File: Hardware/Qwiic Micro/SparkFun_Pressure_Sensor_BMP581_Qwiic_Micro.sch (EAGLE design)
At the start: 28 parts, among them J1 QWIIC_RIGHT_ANGLE, U1 BMP581

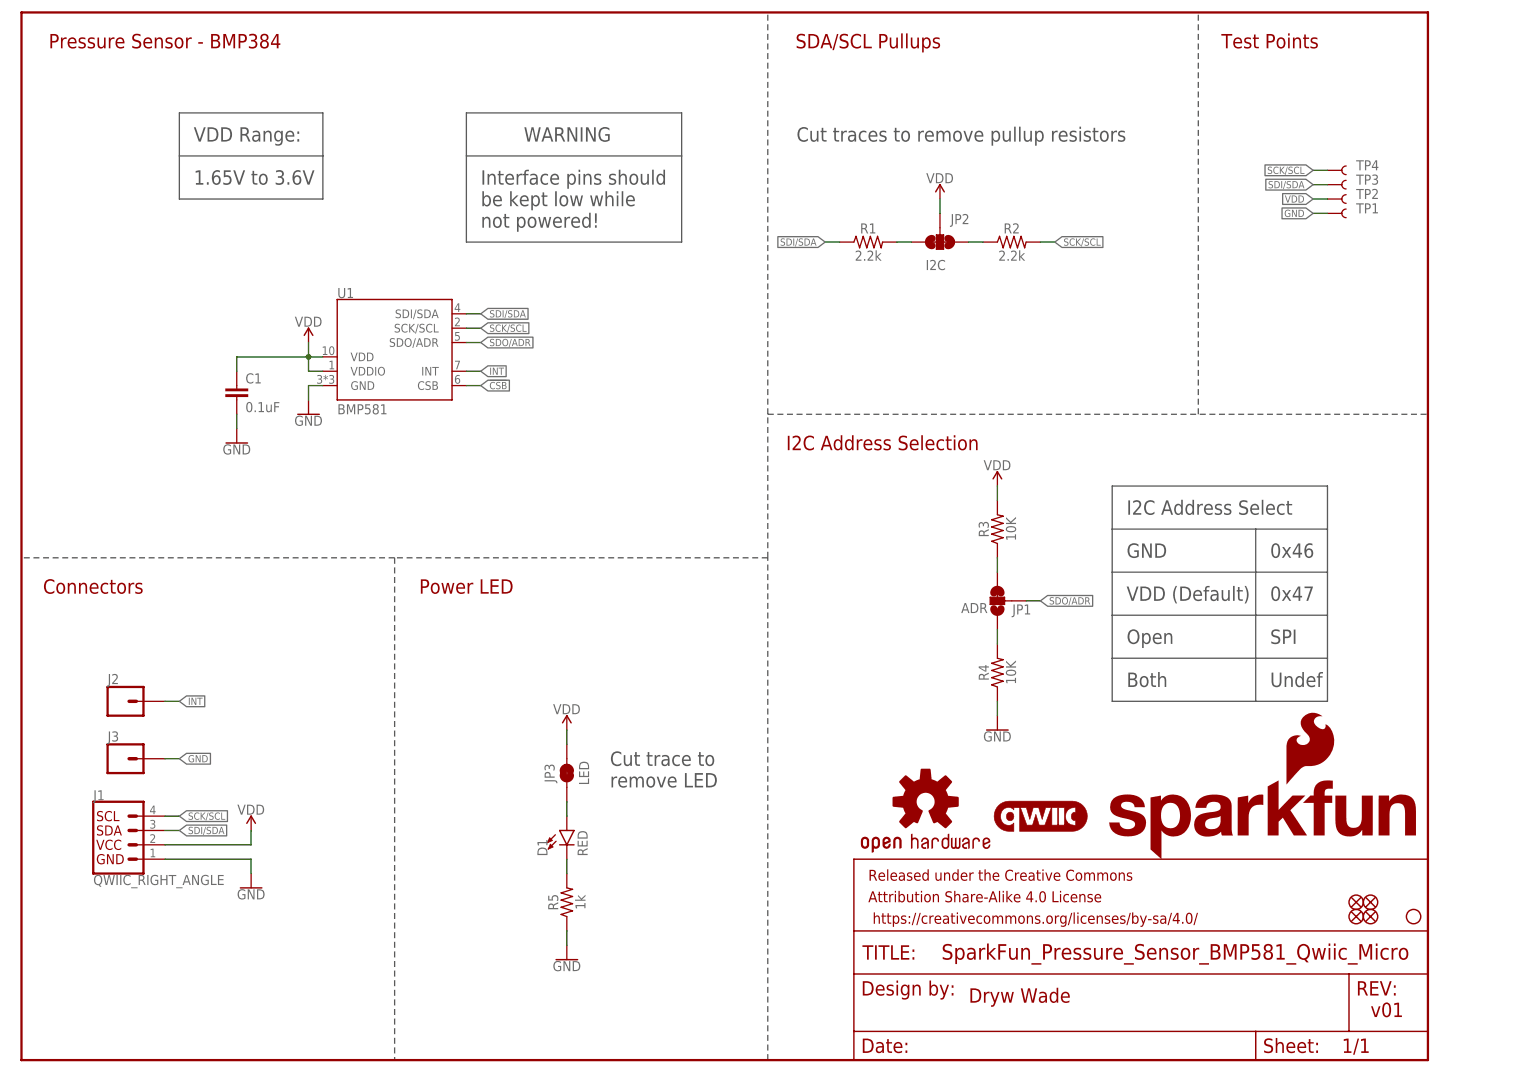
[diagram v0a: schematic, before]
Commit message: Design review updates
Rename files
Change to v10 (accelerating to reds)
Fix sensor name in schematic
Add note to schematic about max wire diameter in Micro PTH connectors
Update VDD range
Fix acid trap in Micro
Move PWR LED to give space
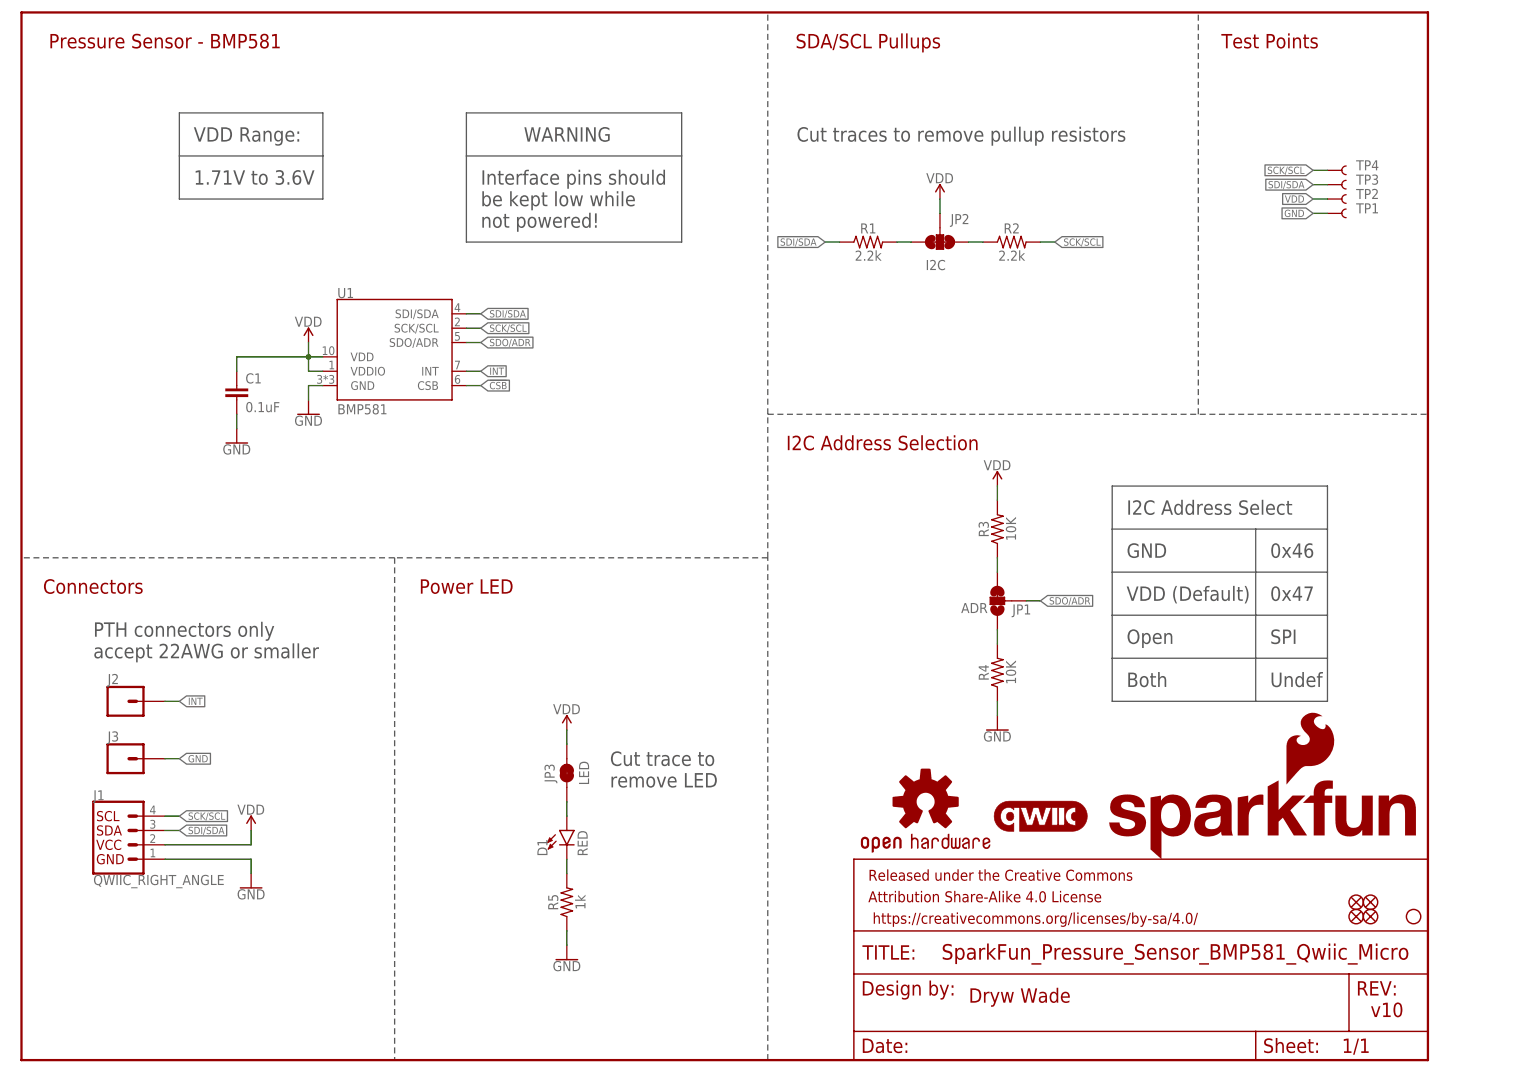
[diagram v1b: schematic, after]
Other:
- note added: "1.71V to 3.6V"
- note added: "PTH connectors only accept 22AWG or smaller"
- note added: "Pressure Sensor - BMP581"
- note added: "v10"
- note removed: "1.65V to 3.6V"
- note removed: "Pressure Sensor - BMP384"
- note removed: "v01"
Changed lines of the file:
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@@
 <plain>
 <text x="167.64" y="10.16" size="2.54" layer="94" font="vector">Dryw Wade</text>
-<text x="238.76" y="7.62" size="2.54" layer="94" font="vector">v01</text>
+<text x="238.76" y="7.62" size="2.54" layer="94" font="vector">v10</text>
 <wire x1="132.08" y1="0" x2="132.08" y2="88.9" width="0.2032" layer="97" style="shortdash"/>
 <wire x1="132.08" y1="88.9" x2="132.08" y2="114.3" width="0.2032" layer="97" style="shortdash"/>
 <wire x1="132.08" y1="114.3" x2="132.08" y2="185.42" width="0.2032" layer="97" style="shortdash"/>
 <wire x1="132.08" y1="88.9" x2="66.04" y2="88.9" width="0.2032" layer="97" style="shortdash"/>
-<text x="25.4" y="180.34" size="2.54" layer="94" font="vector" align="center">Pressure Sensor - BMP384</text>
+<text x="25.4" y="180.34" size="2.54" layer="94" font="vector" align="center">Pressure Sensor - BMP581</text>
 <text x="152.4" y="109.22" size="2.54" layer="94" font="vector" align="center">I2C Address Selection</text>
 <text x="195.58" y="96.52" size="2.54" layer="97" font="vector">I2C Address Select</text>
@@
 <wire x1="132.08" y1="114.3" x2="248.92" y2="114.3" width="0.2032" layer="97" style="shortdash"/>
 <text x="30.48" y="162.56" size="2.54" layer="97" font="vector">VDD Range:</text>
-<text x="30.48" y="154.94" size="2.54" layer="97" font="vector">1.65V to 3.6V</text>
+<text x="30.48" y="154.94" size="2.54" layer="97" font="vector">1.71V to 3.6V</text>
 <wire x1="27.94" y1="167.64" x2="27.94" y2="160.02" width="0.2032" layer="97"/>
 <wire x1="27.94" y1="160.02" x2="27.94" y2="152.4" width="0.2032" layer="97"/>
@@
 <text x="104.14" y="48.26" size="2.54" layer="97" font="vector">Cut trace to
 remove LED</text>
+<text x="12.7" y="71.12" size="2.54" layer="97" font="vector">PTH connectors only
+accept 22AWG or smaller</text>
 </plain>
 <instances>

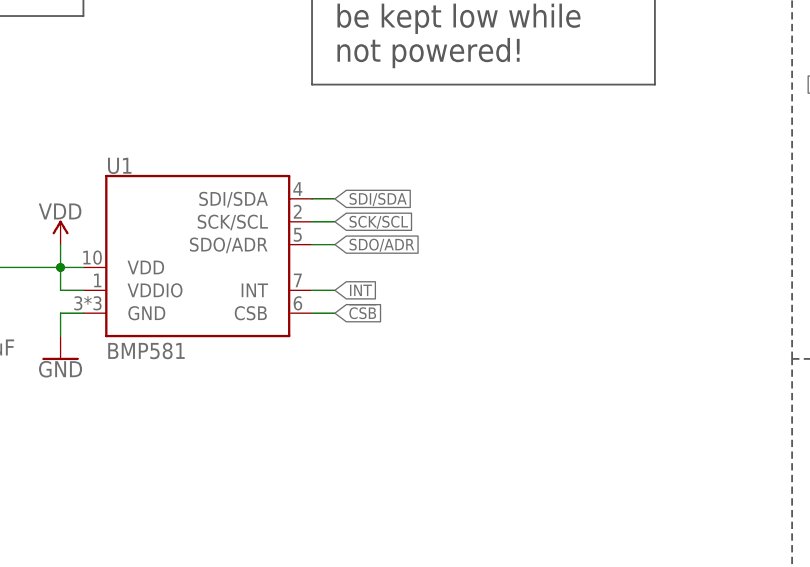
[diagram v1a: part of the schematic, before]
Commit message: Connect CSB of Micro board to VDD
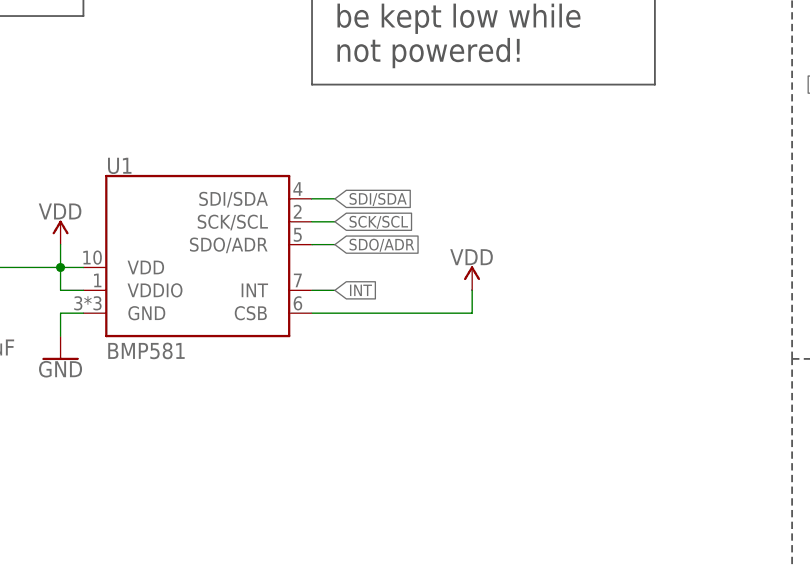
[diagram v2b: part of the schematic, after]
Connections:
- removed net !CSB!: U1.CSB
- net VDD: now also U1.CSB
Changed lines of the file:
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@@
 <part name="R4" library="SparkFun-Resistors" deviceset="10KOHM" device="-0402-1/10W-0.1%" value="10K"/>
 <part name="GND6" library="SparkFun-PowerSymbols" deviceset="GND" device=""/>
+<part name="SUPPLY3" library="SparkFun-PowerSymbols" deviceset="VDD" device=""/>
 </parts>
 <sheets>
@@
 <attribute name="VALUE" x="172.72" y="58.166" size="1.778" layer="96" align="top-center"/>
 </instance>
+<instance part="SUPPLY3" gate="VDD" x="96.52" y="121.92" smashed="yes">
+<attribute name="VALUE" x="96.52" y="124.714" size="1.778" layer="96" align="bottom-center"/>
+</instance>
 </instances>
 <busses>
@@
 <pinref part="SUPPLY7" gate="VDD" pin="VDD"/>
 </segment>
+<segment>
+<pinref part="SUPPLY3" gate="VDD" pin="VDD"/>
+<wire x1="78.74" y1="119.38" x2="96.52" y2="119.38" width="0.1524" layer="91"/>
+<wire x1="96.52" y1="119.38" x2="96.52" y2="121.92" width="0.1524" layer="91"/>
+<pinref part="U1" gate="G$1" pin="CSB"/>
+</segment>
 </net>
 <net name="GND" class="0">
@@
 </segment>
 </net>
-<net name="!CSB!" class="0">
-<segment>
-<wire x1="78.74" y1="119.38" x2="81.28" y2="119.38" width="0.1524" layer="91"/>
-<label x="81.28" y="119.38" size="1.27" layer="95" font="vector" xref="yes"/>
-<pinref part="U1" gate="G$1" pin="CSB"/>
-</segment>
-</net>

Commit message: Design review updates
Change INT label to fishtail in Micro silk
Add product name to bottom in 1x1 silk
Change Micro net labels to be I2C only
Approve DRC overlaps
Fix acid trap
Add note about CSB being tied high in Micro schematic
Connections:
- net SCK/SCL renamed SCL
- net SDI/SDA renamed SDA
- net SDO/ADR renamed ADR
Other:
- note added: "CSB tied to VDD to prevent switching to SPI"
- moved on the sheet: JP2, R1, R2
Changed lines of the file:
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@@
 <text x="12.7" y="83.82" size="2.54" layer="94" font="vector" align="center">Connectors</text>
 <text x="149.86" y="180.34" size="2.54" layer="94" font="vector" align="center">SDA/SCL Pullups</text>
-<text x="137.16" y="162.56" size="2.54" layer="97" font="vector">Cut traces to remove pullup resistors</text>
+<text x="142.24" y="162.56" size="2.54" layer="97" font="vector">Cut traces to remove pullup resistors</text>
 <wire x1="208.28" y1="114.3" x2="208.28" y2="185.42" width="0.2032" layer="97" style="shortdash"/>
 <text x="220.98" y="180.34" size="2.54" layer="94" font="vector" align="center">Test Points</text>
@@
 <text x="12.7" y="71.12" size="2.54" layer="97" font="vector">PTH connectors only
 accept 22AWG or smaller</text>
+<text x="81.28" y="106.68" size="2.54" layer="97" font="vector">CSB tied to VDD to
+prevent switching to SPI</text>
 </plain>
 <instances>
@@
 <attribute name="VALUE" x="96.52" y="17.526" size="1.778" layer="96" align="top-center"/>
 </instance>
-<instance part="R1" gate="G$1" x="149.86" y="144.78" smashed="yes">
-<attribute name="NAME" x="149.86" y="146.304" size="1.778" layer="95" font="vector" align="bottom-center"/>
-<attribute name="VALUE" x="149.86" y="143.256" size="1.778" layer="96" font="vector" align="top-center"/>
-</instance>
-<instance part="R2" gate="G$1" x="175.26" y="144.78" smashed="yes">
-<attribute name="NAME" x="175.26" y="146.304" size="1.778" layer="95" font="vector" align="bottom-center"/>
-<attribute name="VALUE" x="175.26" y="143.256" size="1.778" layer="96" font="vector" align="top-center"/>
-</instance>
-<instance part="SUPPLY5" gate="VDD" x="162.56" y="152.4" smashed="yes">
-<attribute name="VALUE" x="162.56" y="155.194" size="1.778" layer="96" align="bottom-center"/>
-</instance>
-<instance part="JP2" gate="G$1" x="162.56" y="144.78" smashed="yes" rot="R270">
-<attribute name="NAME" x="166.116" y="148.844" size="1.778" layer="95" font="vector" align="center"/>
-<attribute name="VALUE" x="161.798" y="140.716" size="1.778" layer="96" font="vector" align="center"/>
+<instance part="R1" gate="G$1" x="157.48" y="144.78" smashed="yes">
+<attribute name="NAME" x="157.48" y="146.304" size="1.778" layer="95" font="vector" align="bottom-center"/>
+<attribute name="VALUE" x="157.48" y="143.256" size="1.778" layer="96" font="vector" align="top-center"/>
+</instance>
+<instance part="R2" gate="G$1" x="182.88" y="144.78" smashed="yes">
+<attribute name="NAME" x="182.88" y="146.304" size="1.778" layer="95" font="vector" align="bottom-center"/>
+<attribute name="VALUE" x="182.88" y="143.256" size="1.778" layer="96" font="vector" align="top-center"/>
+</instance>
+<instance part="SUPPLY5" gate="VDD" x="170.18" y="152.4" smashed="yes">
+<attribute name="VALUE" x="170.18" y="155.194" size="1.778" layer="96" align="bottom-center"/>
+</instance>
+<instance part="JP2" gate="G$1" x="170.18" y="144.78" smashed="yes" rot="R270">
+<attribute name="NAME" x="173.736" y="148.844" size="1.778" layer="95" font="vector" align="center"/>
+<attribute name="VALUE" x="169.418" y="140.716" size="1.778" layer="96" font="vector" align="center"/>
 </instance>
 <instance part="C1" gate="G$1" x="38.1" y="116.84" smashed="yes">
@@
 <pinref part="JP2" gate="G$1" pin="2"/>
 <pinref part="SUPPLY5" gate="VDD" pin="VDD"/>
-<wire x1="162.56" y1="149.86" x2="162.56" y2="152.4" width="0.1524" layer="91"/>
+<wire x1="170.18" y1="149.86" x2="170.18" y2="152.4" width="0.1524" layer="91"/>
 </segment>
 <segment>
@@
 </segment>
 </net>
-<net name="SDI/SDA" class="0">
+<net name="SDA" class="0">
 <segment>
 <label x="81.28" y="132.08" size="1.27" layer="95" font="vector" xref="yes"/>
@@
 <segment>
 <pinref part="R1" gate="G$1" pin="1"/>
-<wire x1="142.24" y1="144.78" x2="144.78" y2="144.78" width="0.1524" layer="91"/>
-<label x="142.24" y="144.78" size="1.27" layer="95" font="vector" rot="R180" xref="yes"/>
-</segment>
-</net>
-<net name="SCK/SCL" class="0">
+<wire x1="149.86" y1="144.78" x2="152.4" y2="144.78" width="0.1524" layer="91"/>
+<label x="149.86" y="144.78" size="1.27" layer="95" font="vector" rot="R180" xref="yes"/>
+</segment>
+</net>
+<net name="SCL" class="0">
 <segment>
 <wire x1="78.74" y1="129.54" x2="81.28" y2="129.54" width="0.1524" layer="91"/>
@@
 <segment>
 <pinref part="R2" gate="G$1" pin="2"/>
-<wire x1="180.34" y1="144.78" x2="182.88" y2="144.78" width="0.1524" layer="91"/>
-<label x="182.88" y="144.78" size="1.27" layer="95" font="vector" xref="yes"/>
-</segment>
-</net>
-<net name="SDO/ADR" class="0">
+<wire x1="187.96" y1="144.78" x2="190.5" y2="144.78" width="0.1524" layer="91"/>
+<label x="190.5" y="144.78" size="1.27" layer="95" font="vector" xref="yes"/>
+</segment>
+</net>
+<net name="ADR" class="0">
 <segment>
 <wire x1="78.74" y1="127" x2="81.28" y2="127" width="0.1524" layer="91"/>
@@
 <pinref part="R2" gate="G$1" pin="1"/>
 <pinref part="JP2" gate="G$1" pin="1"/>
-<wire x1="170.18" y1="144.78" x2="167.64" y2="144.78" width="0.1524" layer="91"/>
+<wire x1="177.8" y1="144.78" x2="175.26" y2="144.78" width="0.1524" layer="91"/>
 </segment>
 </net>
@@
 <pinref part="JP2" gate="G$1" pin="3"/>
 <pinref part="R1" gate="G$1" pin="2"/>
-<wire x1="157.48" y1="144.78" x2="154.94" y2="144.78" width="0.1524" layer="91"/>
-</segment>
-</net>
+<wire x1="165.1" y1="144.78" x2="162.56" y2="144.78" width="0.1524" layer="91"/>
+</segment>
+</net>

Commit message: Remove library file
BMP384 is in SFE Eagle library, update part in design
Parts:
- U1: device BMP581:BMP581 -> SparkFun-Sensors:BMP581
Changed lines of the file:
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@@
 <part name="H1" library="SparkFun-Hardware" deviceset="STAND-OFF" device=""/>
 <part name="GND4" library="SparkFun-PowerSymbols" deviceset="GND" device=""/>
-<part name="U1" library="BMP581" deviceset="BMP581" device=""/>
+<part name="U1" library="SparkFun-Sensors" deviceset="BMP581" device=""/>
 <part name="J1" library="SparkFun-Connectors" deviceset="QWIIC_CONNECTOR" device="JS-1MM" value="QWIIC_RIGHT_ANGLE"/>
 <part name="GND2" library="SparkFun-PowerSymbols" deviceset="GND" device=""/>
